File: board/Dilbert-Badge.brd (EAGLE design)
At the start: 106.7 x 52.1 mm, 47 parts, among them IC1 MCP23017SO, J1 IO EXP., J2 FTDI_DEVICE, J3 NEOPIXEL, J4 PWR IN, J5 I2C, SW1 UP, SW2 DOWN, SW3 LEFT, SW4 RIGHT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

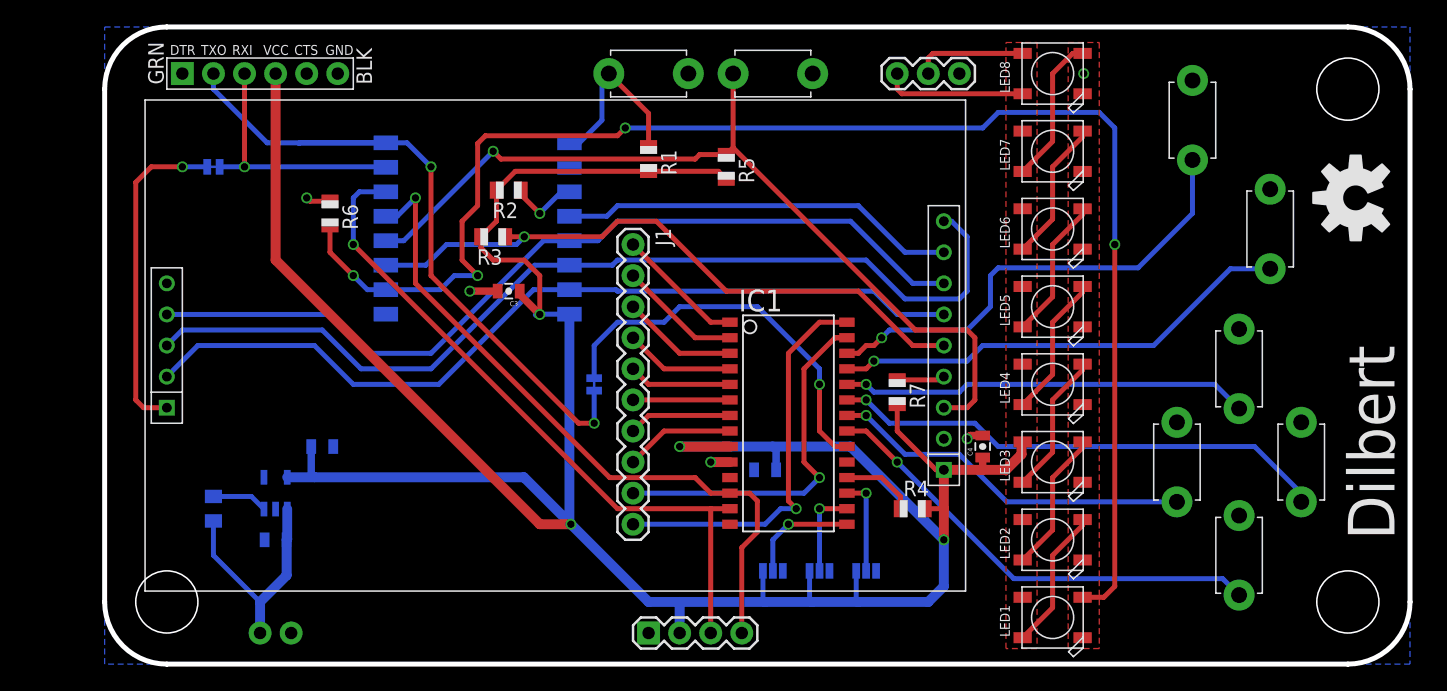
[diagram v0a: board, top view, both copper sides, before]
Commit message: Moved layout for better hold position.
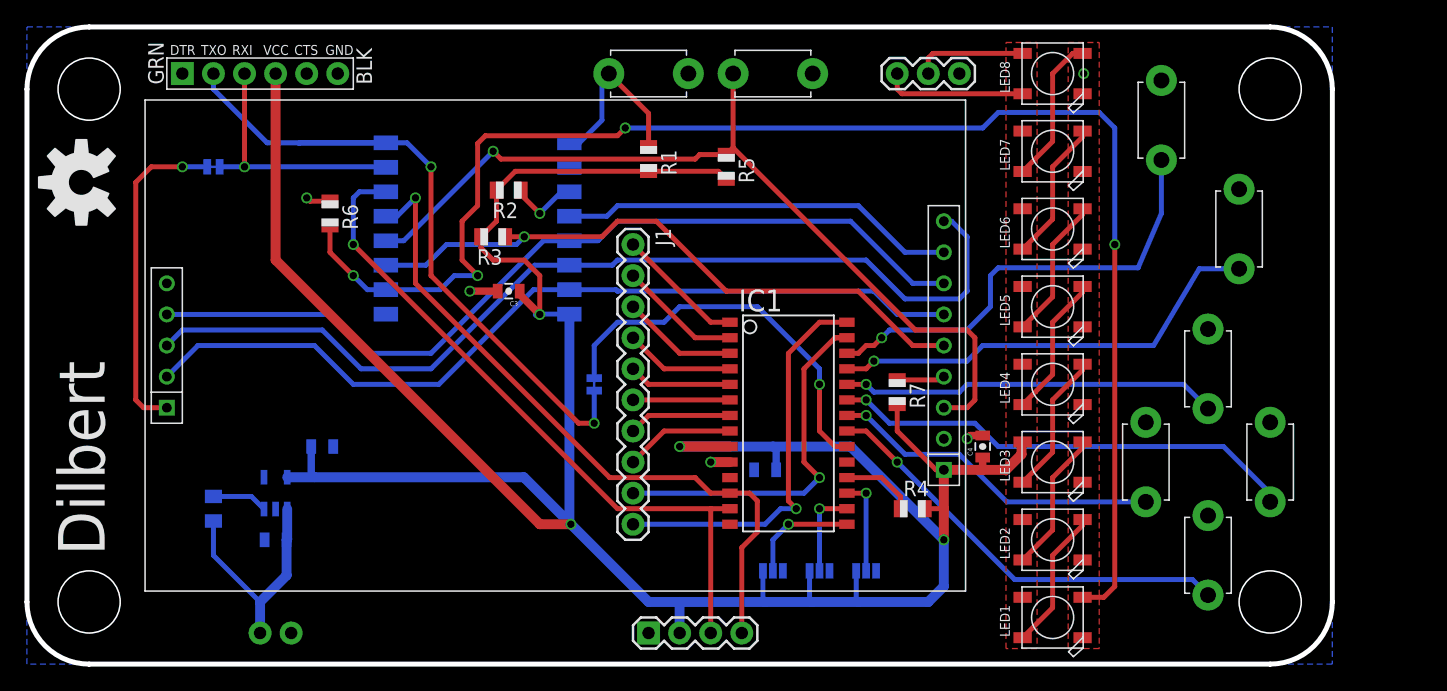
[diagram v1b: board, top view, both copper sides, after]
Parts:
- added U$5: 5MM_MOUNTING_HOLE, mechanical:5MM_HOLE
- moved LOGO1 104.1 mm to (-4.45, 44.5)
- moved SW3 15.5 mm to (87.6, 29.2)
- moved SW4 15.5 mm to (87.6, 14.0)
- moved U$2 6.35 mm to (92.7, 10.2)
- moved U$3 6.35 mm to (92.7, 52.1)
- moved U$4 6.35 mm to (-3.81, 10.2)
- moved SW1 2.54 mm to (82.5, 21.6)
- moved SW2 2.54 mm to (92.7, 21.6)
- moved SW6 2.54 mm to (83.8, 49.5)
- moved SW5 2.54 mm to (90.2, 40.6)
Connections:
- net BTN_L: now also IC1.24; no longer IC1.21
- net BTN_R: now also IC1.21; no longer IC1.24
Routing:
- net BTN_L: track 37.6 -> 30.9 mm
- net BTN_U: track 29.9 -> 27.4 mm
- net BTN_D: track 41.0 -> 38.5 mm
- net BTN_R: track 33.4 -> 35.1 mm
- net BTN_A: track 38.0 -> 36.4 mm
- net BTN_B: track 38.8 -> 37.4 mm

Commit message: Revert "Moved layout for better hold position."
This reverts commit 4734362e310bc9f544577fd27d433fa3af5f158a.
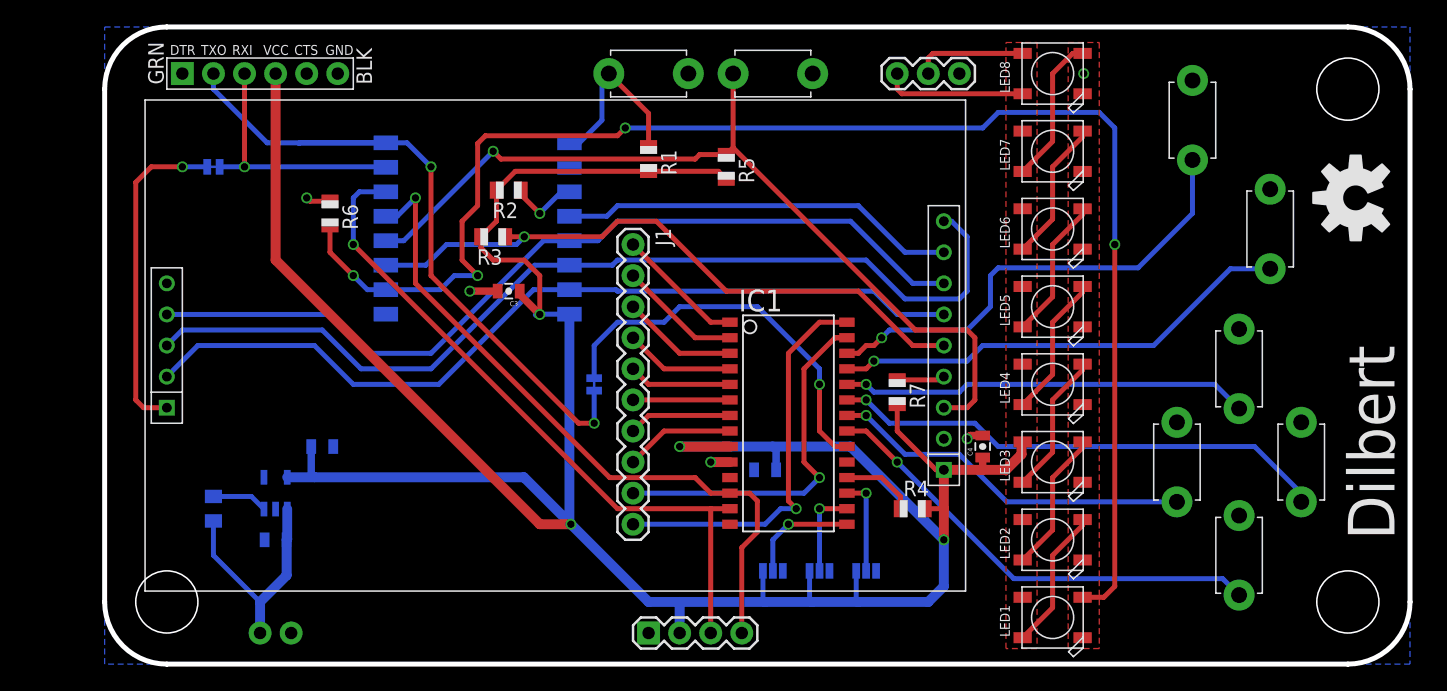
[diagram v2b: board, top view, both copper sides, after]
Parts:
- removed U$5: 5MM_MOUNTING_HOLE, mechanical:5MM_HOLE
- moved LOGO1 104.1 mm to (99.7, 43.2)
- moved SW3 15.5 mm to (90.2, 14.0)
- moved SW4 15.5 mm to (90.2, 29.2)
- moved U$2 6.35 mm to (99.1, 10.2)
- moved U$3 6.35 mm to (99.1, 52.1)
- moved U$4 6.35 mm to (2.54, 10.2)
- moved SW1 2.54 mm to (85.1, 21.6)
- moved SW2 2.54 mm to (95.2, 21.6)
- moved SW6 2.54 mm to (86.4, 49.5)
- moved SW5 2.54 mm to (92.7, 40.6)
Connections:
- net BTN_L: now also IC1.21; no longer IC1.24
- net BTN_R: now also IC1.24; no longer IC1.21
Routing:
- net BTN_L: track 30.9 -> 37.6 mm
- net BTN_U: track 27.4 -> 29.9 mm
- net BTN_D: track 38.5 -> 41.0 mm
- net BTN_R: track 35.1 -> 33.4 mm
- net BTN_A: track 36.4 -> 38.0 mm
- net BTN_B: track 37.4 -> 38.8 mm

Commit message: Redo Alistair's new layout
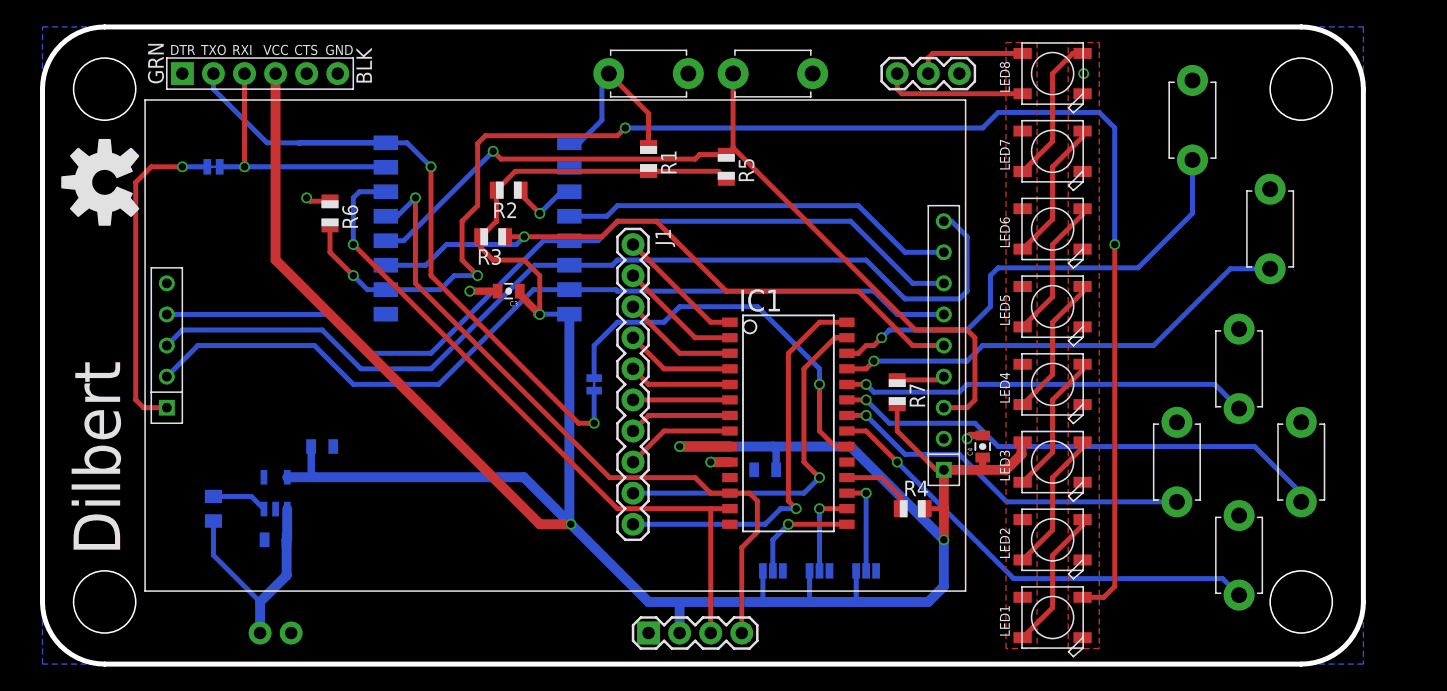
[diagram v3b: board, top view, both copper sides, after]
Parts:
- added U$5: 5MM_MOUNTING_HOLE, mechanical:5MM_HOLE
- moved LOGO1 102.2 mm to (-2.54, 44.5)
- moved U$4 5.08 mm to (-2.54, 10.2)
- moved U$2 3.81 mm to (95.2, 10.2)
- moved U$3 3.81 mm to (95.2, 52.1)
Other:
- board size 106.7 x 52.1 mm -> 108 x 52.1 mm
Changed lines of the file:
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@@
 <board>
 <plain>
-<wire x1="2.54" y1="57.15" x2="99.06" y2="57.15" width="0.4064" layer="20"/>
-<wire x1="-2.54" y1="52.07" x2="-2.54" y2="10.16" width="0.4064" layer="20"/>
-<wire x1="2.54" y1="5.08" x2="99.06" y2="5.08" width="0.4064" layer="20"/>
-<wire x1="104.14" y1="10.16" x2="104.14" y2="52.07" width="0.4064" layer="20"/>
-<wire x1="-2.54" y1="52.07" x2="2.54" y2="57.15" width="0.4064" layer="20" curve="-90"/>
-<wire x1="2.54" y1="5.08" x2="-2.54" y2="10.16" width="0.4064" layer="20" curve="-90"/>
-<wire x1="104.14" y1="10.16" x2="99.06" y2="5.08" width="0.4064" layer="20" curve="-90"/>
-<wire x1="99.06" y1="57.15" x2="104.14" y2="52.07" width="0.4064" layer="20" curve="-90"/>
-<text x="102.87" y="15.24" size="3.81" layer="25" rot="R90">Dilbert</text>
-<text x="100.33" y="31.75" size="1.27" layer="27" rot="R90">2016</text>
+<wire x1="-2.54" y1="57.15" x2="95.25" y2="57.15" width="0.4064" layer="20"/>
+<wire x1="-7.62" y1="52.07" x2="-7.62" y2="10.16" width="0.4064" layer="20"/>
+<wire x1="-2.54" y1="5.08" x2="95.25" y2="5.08" width="0.4064" layer="20"/>
+<wire x1="100.33" y1="10.16" x2="100.33" y2="52.07" width="0.4064" layer="20"/>
+<wire x1="-7.62" y1="52.07" x2="-2.54" y2="57.15" width="0.4064" layer="20" curve="-90"/>
+<wire x1="-2.54" y1="5.08" x2="-7.62" y2="10.16" width="0.4064" layer="20" curve="-90"/>
+<wire x1="100.33" y1="10.16" x2="95.25" y2="5.08" width="0.4064" layer="20" curve="-90"/>
+<wire x1="95.25" y1="57.15" x2="100.33" y2="52.07" width="0.4064" layer="20" curve="-90"/>
+<text x="-1.27" y="13.97" size="3.81" layer="25" rot="R90">Dilbert</text>
+<text x="-1.27" y="31.75" size="1.27" layer="27" rot="R90">2016</text>
 <text x="67.31" y="51.435" size="1.27" layer="28" rot="MR270" align="center-left">GND</text>
 <text x="64.77" y="51.435" size="1.27" layer="28" rot="MR270" align="center-left">3V3</text>
@@
 <attribute name="VALUE" x="55.086" y="56.426" size="0.8128" layer="27" ratio="10" rot="R180"/>
 </element>
-<element name="LOGO1" library="SparkFun-Aesthetics" package="OSHW-LOGO-L" value="OSHW-LOGOL" x="99.695" y="43.18" rot="R90"/>
+<element name="LOGO1" library="SparkFun-Aesthetics" package="OSHW-LOGO-L" value="OSHW-LOGOL" x="-2.54" y="44.45" rot="R90"/>
 <element name="R1" library="adafruit" package="R0805" value="10K" x="41.91" y="46.355" rot="R270"/>
 <element name="R2" library="adafruit" package="R0805" value="10K" x="30.48" y="43.815" rot="R180"/>
@@
 <element name="JP4" library="SparkFun-Passives" package="PAD-JUMPER-2-NC_BY_TRACE_NO_SILK" value="IO INT TO UART TX" x="37.465" y="27.94" rot="MR90"/>
 <element name="JP5" library="SparkFun-Passives" package="PAD-JUMPER-2-NC_BY_TRACE_NO_SILK" value="SD CS TO UART RX" x="6.35" y="45.72" rot="MR0"/>
-<element name="U$2" library="mechanical" package="5MM_HOLE" value="5MM_MOUNTING_HOLE" x="99.06" y="10.16"/>
-<element name="U$3" library="mechanical" package="5MM_HOLE" value="5MM_MOUNTING_HOLE" x="99.06" y="52.07"/>
+<element name="U$2" library="mechanical" package="5MM_HOLE" value="5MM_MOUNTING_HOLE" x="95.25" y="10.16"/>
+<element name="U$3" library="mechanical" package="5MM_HOLE" value="5MM_MOUNTING_HOLE" x="95.25" y="52.07"/>
 <element name="J1" library="SparkFun-Connectors" package="1X10" value="IO EXP." x="40.64" y="39.37" rot="R270">
 <attribute name="PROD_ID" value="CONN-11563" x="40.64" y="39.37" size="1.778" layer="27" rot="R270" display="off"/>
@@
 <attribute name="PROD_ID" value="CAP-11625" x="55.245" y="26.035" size="1.016" layer="28" rot="MR0" display="off"/>
 </element>
-<element name="U$4" library="mechanical" package="5MM_HOLE" value="5MM_MOUNTING_HOLE" x="2.54" y="10.16"/>
+<element name="U$4" library="mechanical" package="5MM_HOLE" value="5MM_MOUNTING_HOLE" x="-2.54" y="10.16"/>
+<element name="U$5" library="mechanical" package="5MM_HOLE" value="5MM_MOUNTING_HOLE" x="-2.54" y="52.07"/>
 </elements>
 <signals>
@@
 <contactref element="JP2" pad="1"/>
 <polygon width="0.4064" layer="16">
-<vertex x="-2.54" y="57.15"/>
-<vertex x="104.14" y="57.15"/>
-<vertex x="104.14" y="5.08"/>
-<vertex x="-2.54" y="5.08"/>
+<vertex x="-7.62" y="57.15"/>
+<vertex x="100.33" y="57.15"/>
+<vertex x="100.33" y="5.08"/>
+<vertex x="-7.62" y="5.08"/>
 </polygon>
 <polygon width="0.4064" layer="1">
